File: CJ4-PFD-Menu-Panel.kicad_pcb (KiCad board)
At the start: 2 copper layers, 122 x 57 mm, 57 parts, among them J1 Conn_01x02, J3 Conn_01x02, J6 USB_B_Micro, J8 Conn_01x02, SW10 SW_PUSH_LED, SW11 SW_PUSH_LED, SW12 SW_PUSH_LED, SW13 SW_PUSH_LED, SW3 SW_PUSH_LED, SW4 SW_PUSH_LED, SW5 SW_PUSH_LED, SW6 SW_PUSH_LED, SW7 SW_PUSH_LED, SW8 SW_PUSH_LED, SW9 SW_PUSH_LED, U1 DM13A, U2 XC6206P332MR, U6 W25Q128JVS, U7 RP2040, Y1 X322512MSB4SI

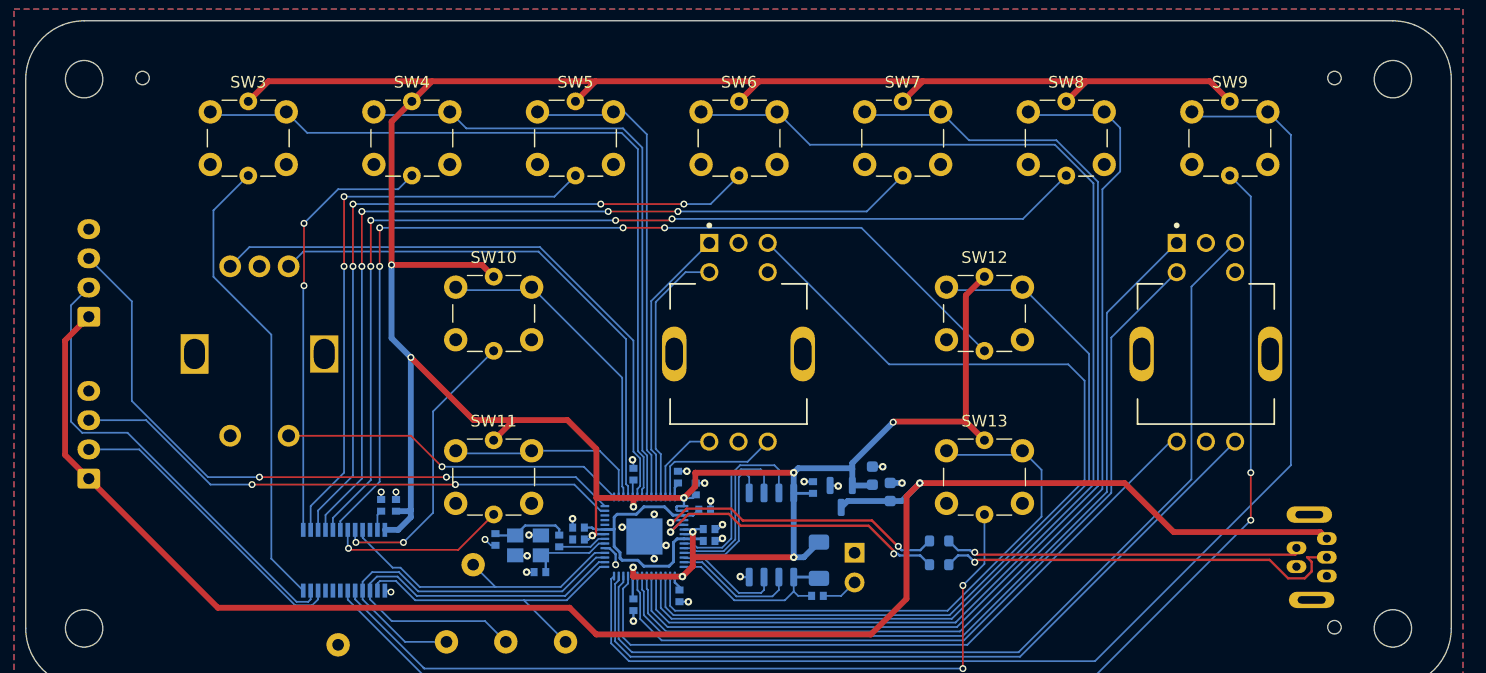
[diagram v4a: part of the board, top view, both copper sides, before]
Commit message: Cleanup silkscreen and version/date
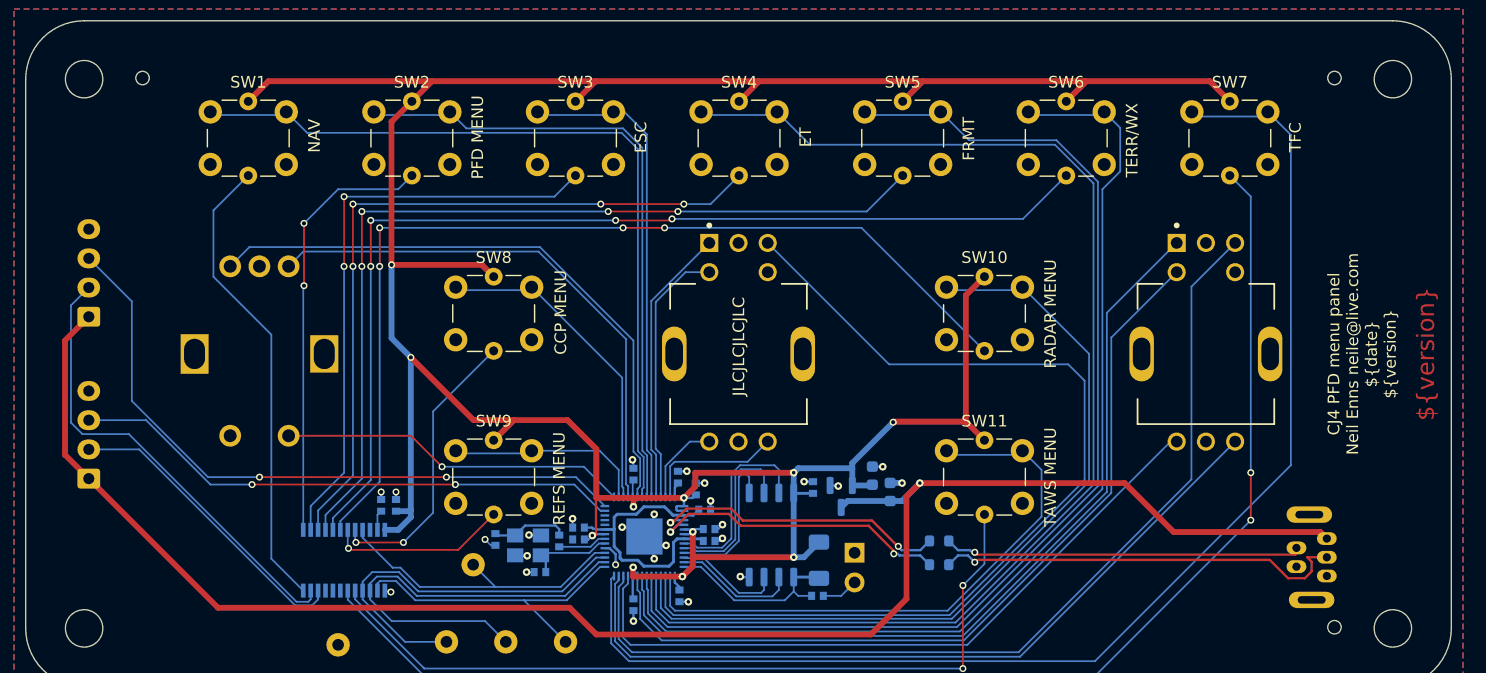
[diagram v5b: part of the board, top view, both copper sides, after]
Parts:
- renumbered J8 to J2, J6 to J4, SW3 to SW1, SW12 to SW10, SW13 to SW11, SW4 to SW2, SW5 to SW3, SW6 to SW4, SW7 to SW5, SW8 to SW6, SW9 to SW7, SW10 to SW8, SW11 to SW9
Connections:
- J1 pad 3: /MASTER_WARNING -> /MASTER_CAUTION
- J2 pad 3: /MASTER_CAUTION -> /MASTER_WARNING
- U7 pad 27: /MASTER_WARNING -> /MASTER_CAUTION
- U7 pad 28: /MASTER_CAUTION -> /MASTER_WARNING
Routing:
- net /MASTER_WARNING: track 47.4 -> 57.9 mm
- net /MASTER_CAUTION: track 57.9 -> 47.4 mm
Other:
- board text added: "${version}"
- board text added: "BRIGHTNESS"
- board text added: "CCP MENU"
- board text added: "CJ4 PFD menu panel Neil Enns neile@live.com ${date} ${version}"
- board text added: "CLOCK"
- board text added: "DIN"
- board text added: "ESC"
- board text added: "ET"
- board text added: "FRMT"
- board text added: "GND"
- board text added: "JLCJLCJLCJLC"
- board text added: "LATCH"
- board text added: "MASTER CAUTION"
- board text added: "MASTER WARNING"
- board text added: "NAV"
- board text added: "PFD MENU"
- board text added: "RADAR MENU"
- board text added: "REFS MENU"
- board text added: "TAWS MENU"
- board text added: "TERR/WX"
- board text added: "TFC"

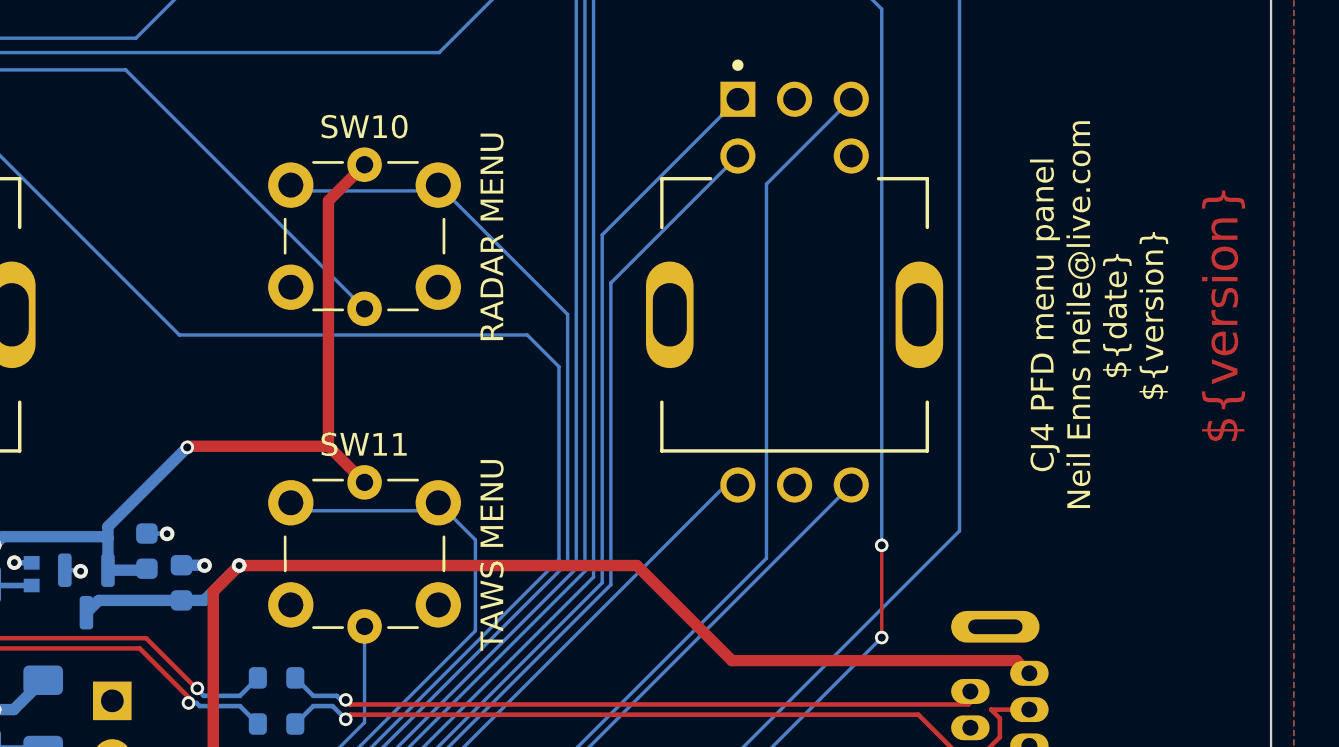
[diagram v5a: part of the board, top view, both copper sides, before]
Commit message: Silkscreen and date/version stuff
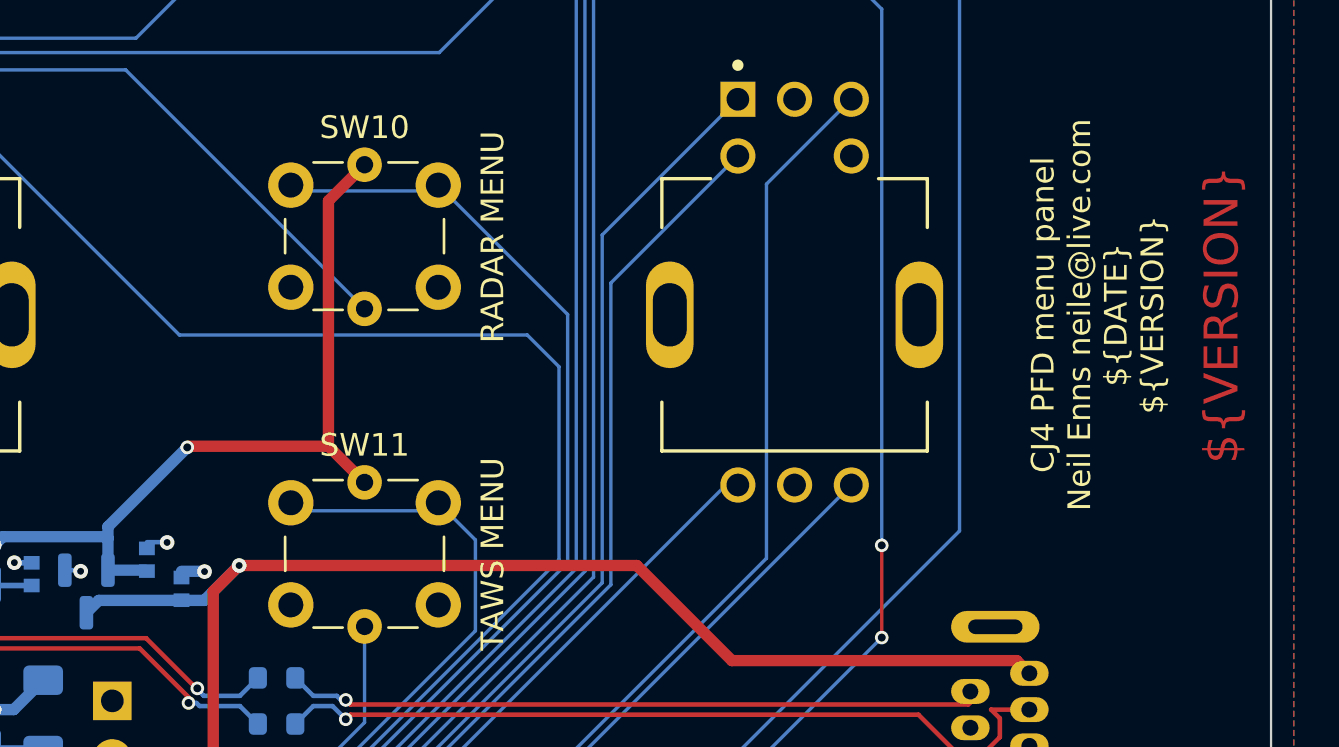
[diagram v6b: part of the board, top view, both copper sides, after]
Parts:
- C1: value 100nF -> 1uF
- C7, C9: footprint Capacitor_SMD:C_0603_1608Metric -> Custom_Footprints:Perfect_0402
- moved C9 0.38 mm to (92.5, 59.3)
- moved C7 0.27 mm to (94.0, 60.6)
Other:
- board text added: "${VERSION}"
- board text added: "CJ4 PFD menu panel Neil Enns neile@live.com ${DATE} ${VERSION}"
- board text removed: "${version}"
- board text removed: "CJ4 PFD menu panel Neil Enns neile@live.com ${date} ${version}"

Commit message: Fix encoder wiring
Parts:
- C8: value 100nF -> 1uF
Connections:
- net /DATA_B renamed /MENU_ADV_B
- net /MENU_ADV_A' renamed /DATA_A'
- net /RANGE_B renamed /TILT_B
- net /TILT_A' renamed /RANGE_A'

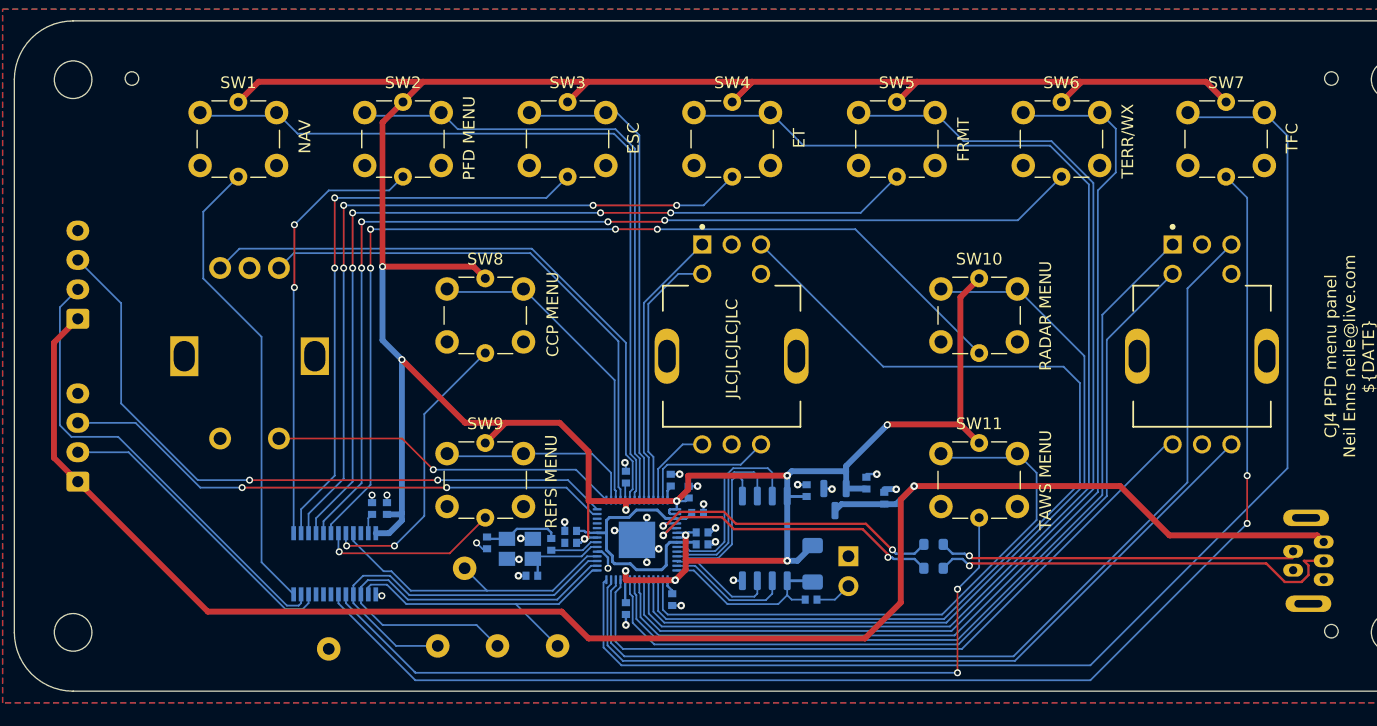
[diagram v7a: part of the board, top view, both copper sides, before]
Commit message: Add debug connections
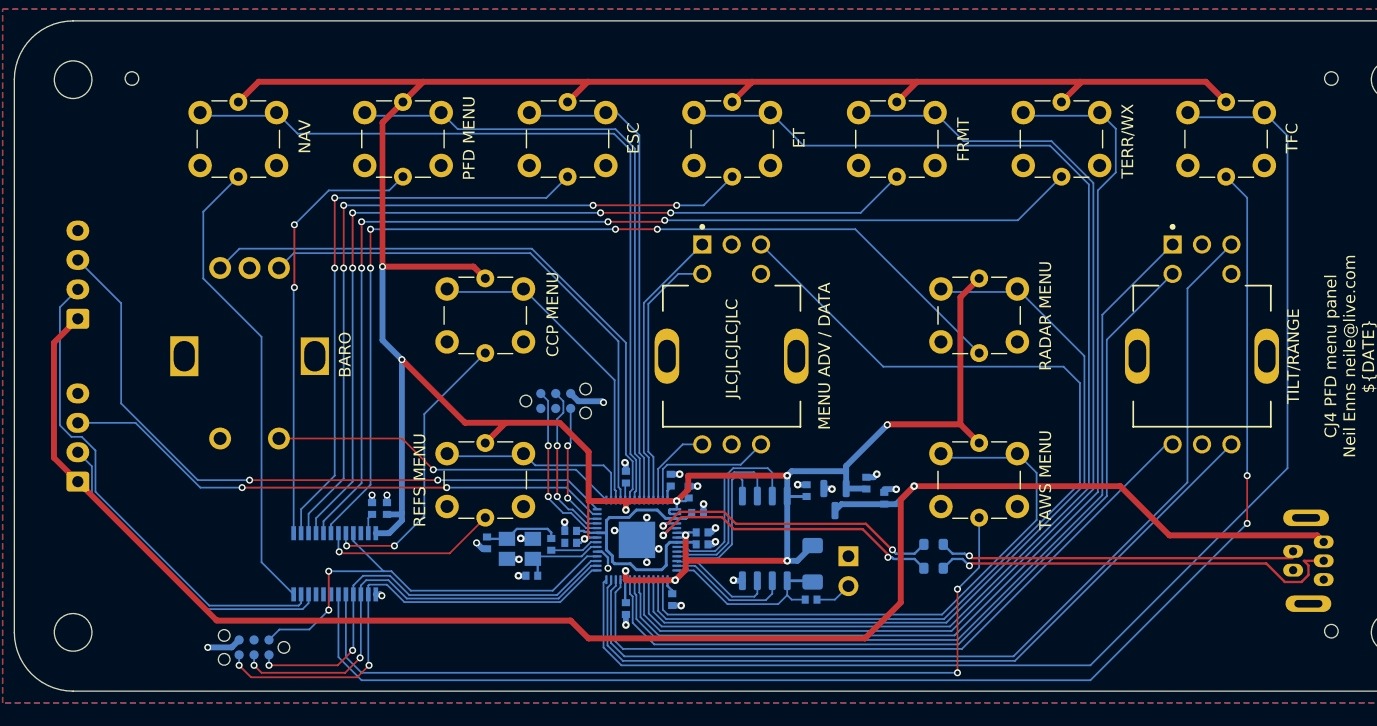
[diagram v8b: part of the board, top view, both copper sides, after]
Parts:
- removed TP1, TP2, TP3, TP4, TP5: TestPoint, TestPoint:TestPoint_Keystone_5000-5004_Miniature
- added J5: RP2040_SWD, Connector:Tag-Connect_TC2030-IDC-NL_2x03_P1.27mm_Vertical, B.Cu at (66.0, 52.3)
- added J6: TC2030-IDC-NL, Connector:Tag-Connect_TC2030-IDC-NL_2x03_P1.27mm_Vertical, B.Cu at (40.4, 73.3)
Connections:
- U7 pad 24: unconnected-(U7-Pad24) -> /RP2040/SWD
- U7 pad 25: unconnected-(U7-Pad25) -> /RP2040/SWCLK
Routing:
- net /RP2040/SWD: track 0.00 -> 14.4 mm, vias 0 -> 2
- net /LED_DIN: track 27.1 -> 40.8 mm, vias 0 -> 2
- net /RP2040/SWCLK: track 0.00 -> 13.7 mm, vias 0 -> 2
- net /BRIGHTNESS: track 27.0 -> 38.5 mm, vias 0 -> 2
- net /RP2040/~{RST}: track 0.00 -> 11.0 mm, vias 0 -> 2
- net GND: track 23.4 -> 29.6 mm, vias 26 -> 28
- net /LED_LATCH: track 33.1 -> 37.0 mm, vias 0 -> 2
- net /LED_TAWS_MENU: track 69.2 -> 71.9 mm
- net /LED_TFC: track 116.5 -> 119.2 mm
- net /LED_CLOCK: track 36.7 -> 39.0 mm, vias 0 -> 2
- net /LED_WARNING: track 39.9 -> 41.9 mm
- net /LED_CAUTION: track 26.1 -> 27.6 mm
- net /TFC: track 109.5 -> 108.4 mm
- net /TAWS_MENU: track 51.0 -> 50.0 mm
- net /PFD_MENU: track 54.5 -> 53.8 mm
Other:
- board text added: "BARO"
- board text added: "BRIGHT NC GND"
- board text added: "LATCH CLOCK DIN"
- board text added: "MENU ADV / DATA"
- board text added: "SWCLK"
- board text added: "SWD"
- board text added: "TILT/RANGE"
- board text removed: "BRIGHTNESS"
- board text removed: "CLOCK"
- board text removed: "DIN"
- board text removed: "LATCH"
